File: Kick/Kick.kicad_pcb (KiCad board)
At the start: 4 copper layers, 11 parts, among them J1 CN1 / J11, J2 CN2 / J12, U0 NOIP1SN1300A-QTI, U1 NOIP1SN1300A-QTI, U2 NX3L4053, U3 NX3L4053, U4 MIC5504-1.8YM5

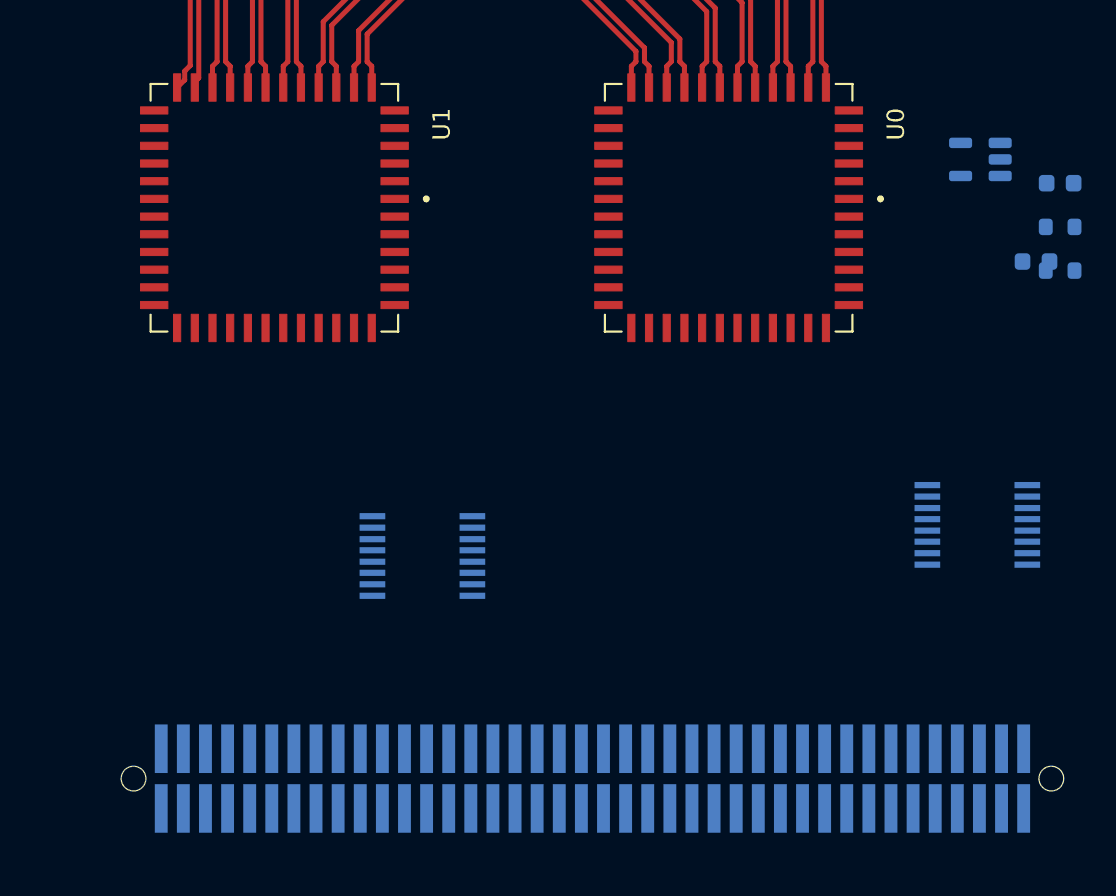
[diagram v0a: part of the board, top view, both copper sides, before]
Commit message: optimized placement of via next to the 2 NOIP2
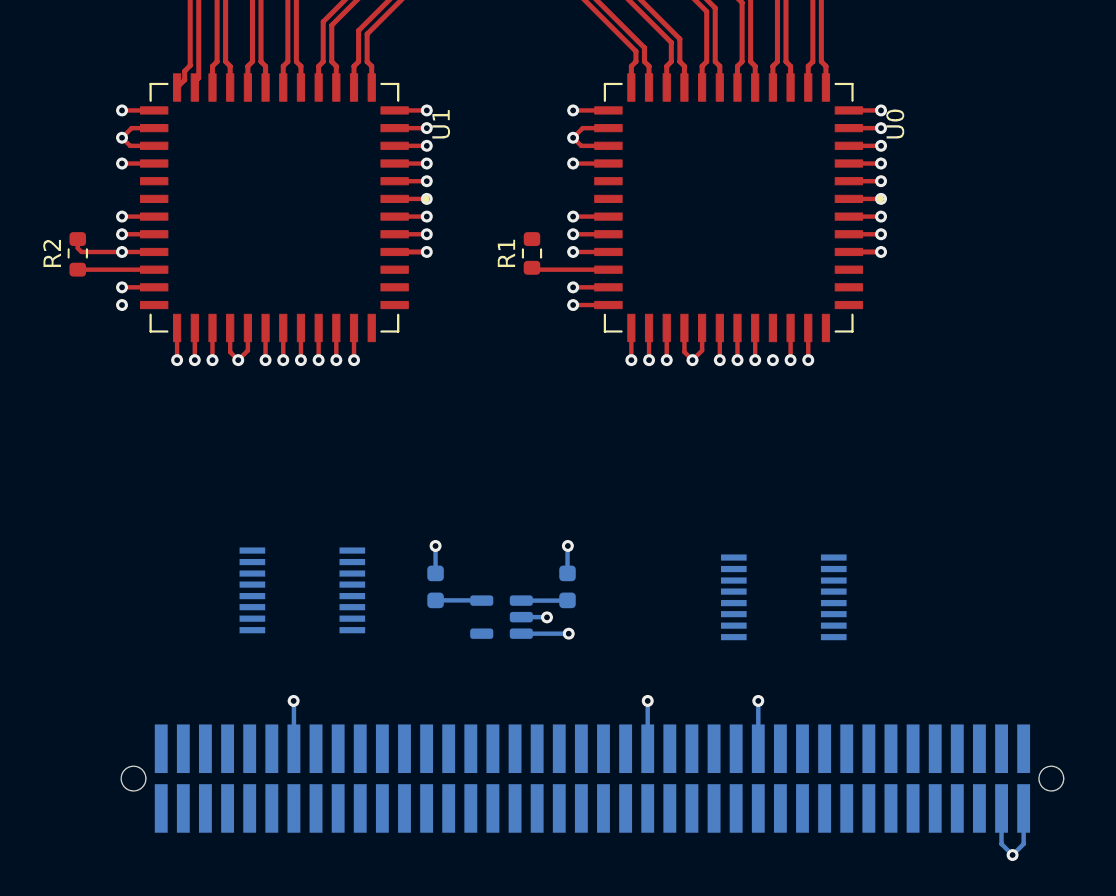
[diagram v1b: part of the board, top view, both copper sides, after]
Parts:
- R1, R2: moved to F.Cu
- moved R2 56.4 mm to (67.0, 72.0), turned to 90 degrees
- moved C2 42.7 mm to (87.6, 91.2), turned to 90 degrees
- moved U3 38.9 mm to (80.0, 91.4), turned to 0 degrees
- moved U4 38.0 mm to (91.4, 92.9)
- moved C1 32.8 mm to (95.2, 91.2), turned to 90 degrees
- moved R1 30.4 mm to (93.1, 72.0), turned to 90 degrees
- moved U2 20.9 mm to (107.6, 91.8)
- moved J1 1.06 mm to (97.1, 102.2), turned to 0 degrees
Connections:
- U0 pad 46: /reset0_N -> /resetn_0
- U2 pad 1: +3.3V -> +3V3
- U2 pad 3: +3.3V -> +3V3
- U3 pad 1: +3.3V -> +3V3
- U3 pad 3: +3.3V -> +3V3
- U4 pad 3: +3.3V -> +3V3
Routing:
- net GND: track 0.00 -> 61.3 mm, vias 0 -> 25
- net /vdd33_0: track 0.00 -> 8.35 mm, vias 0 -> 4
- net /vddpix_0: track 0.00 -> 7.39 mm, vias 0 -> 4
- net /vddpix_1: track 0.00 -> 7.39 mm, vias 0 -> 4
- net /vdd33_1: track 0.00 -> 7.39 mm, vias 0 -> 4
- net /vdd18_0: track 0.00 -> 5.90 mm, vias 0 -> 3
- net /vdd18_1: track 0.00 -> 5.54 mm, vias 0 -> 3
- net +3V3: track 0.00 -> 5.38 mm, vias 0 -> 1
- net Net-(U0-IBIAS_MASTER): track 0.00 -> 4.46 mm
- net Net-(U1-IBIAS_MASTER): track 0.00 -> 4.39 mm
- net /miso: track 0.00 -> 3.74 mm, vias 0 -> 2
- net /sck: track 0.00 -> 3.69 mm, vias 0 -> 2
- net /mosi: track 0.00 -> 3.69 mm, vias 0 -> 2
- net +1V8: track 0.00 -> 2.74 mm
- net /noip_clk_0: track 0.00 -> 2.03 mm, vias 0 -> 1
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- added copper zone on In2.Cu, net +3V3

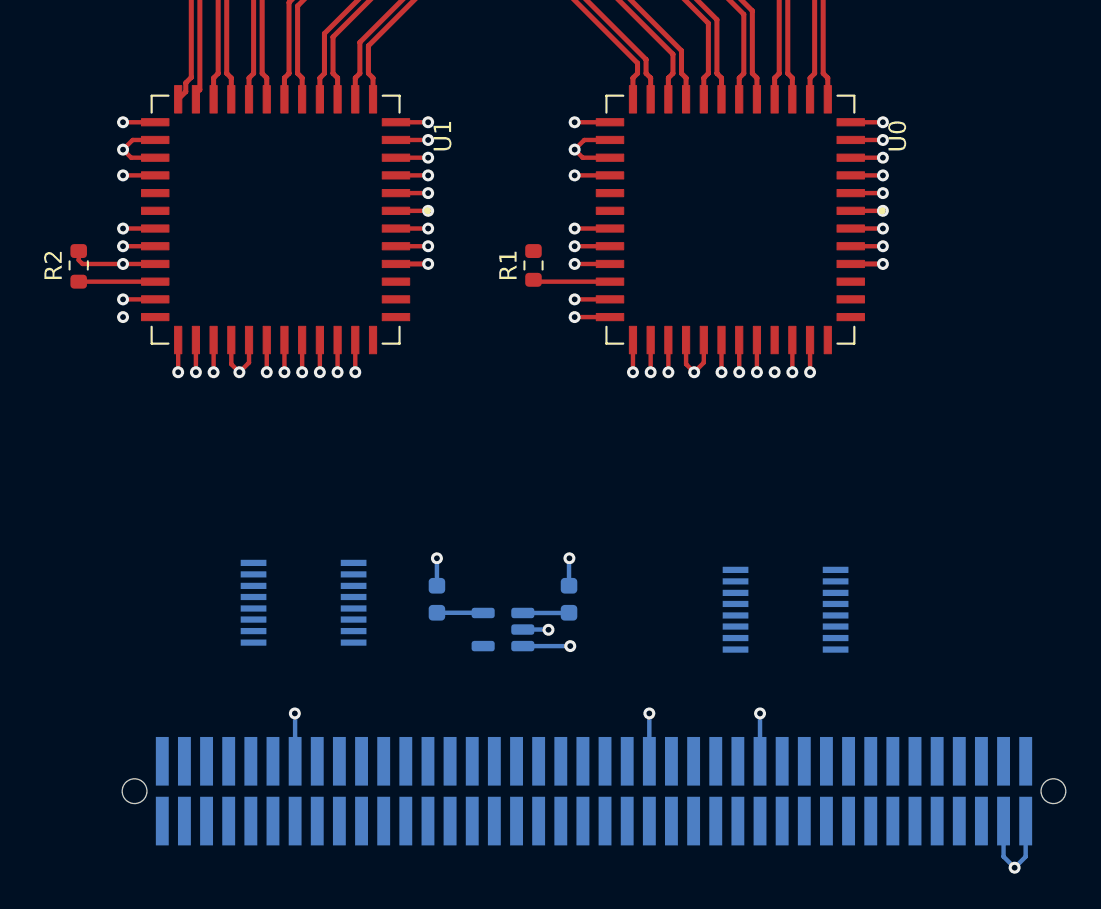
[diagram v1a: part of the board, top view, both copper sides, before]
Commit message: routed U1's side and power supply.
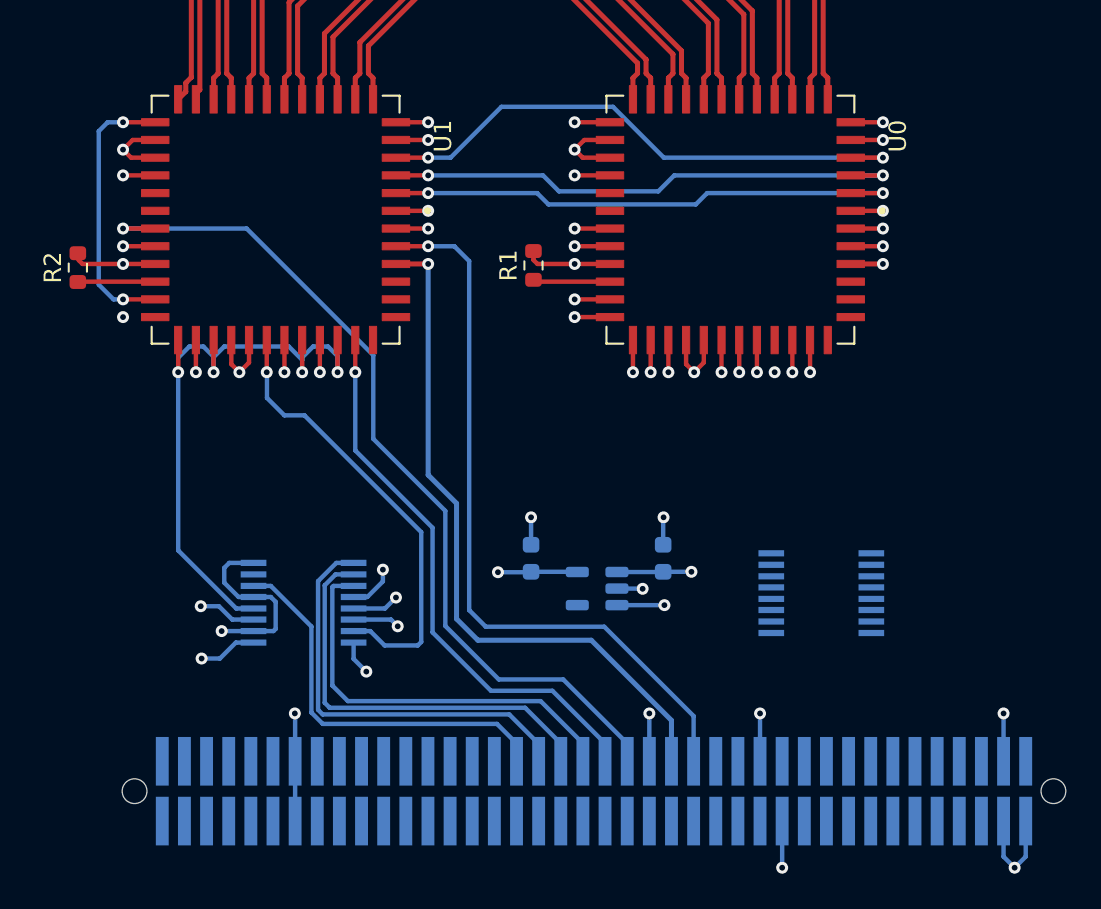
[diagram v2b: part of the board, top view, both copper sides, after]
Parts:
- moved C1 5.89 mm to (100.6, 88.8)
- moved C2 5.89 mm to (93.0, 88.8)
- moved U4 5.89 mm to (96.8, 90.6)
- moved U2 2.26 mm to (109.7, 90.8)
- moved R2 0.13 mm to (67.0, 72.2)
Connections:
- J1 pad 13: /vdd33_toggle_1 -> unconnected-(J1-Pin_13-Pad13)
- J1 pad 19: /vddpix_toggle_1 -> unconnected-(J1-Pin_19-Pad19)
- J1 pad 23: /sw_~{E}_1 -> unconnected-(J1-Pin_23-Pad23)
- J1 pad 28: /noip_clk_1 -> unconnected-(J1-Pin_28-Pad28)
- J1 pad 31: unconnected-(J1-Pin_31-Pad31) -> /ss_1
- J1 pad 32: /trigger0_1 -> unconnected-(J1-Pin_32-Pad32)
- J1 pad 33: unconnected-(J1-Pin_33-Pad33) -> /resetn_1
- J1 pad 37: /mosi -> /noip_clk_1
- J1 pad 38: /resetn_1 -> unconnected-(J1-Pin_38-Pad38)
- J1 pad 39: /miso -> /trigger0_1
- J1 pad 41: /sck -> /vdd18_toggle_1
- J1 pad 43: /ss_0 -> /vdd33_toggle_1
- J1 pad 45: /ss_1 -> /vddpix_toggle_1
- J1 pad 47: unconnected-(J1-Pin_47-Pad47) -> /sw_~{E}_1
- J1 pad 9: /vdd18_toggle_1 -> unconnected-(J1-Pin_9-Pad9)
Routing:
- net /vdd18_1: track 5.54 -> 66.5 mm, vias 3 -> 4
- net /vdd33_1: track 7.39 -> 60.9 mm
- net /noip_clk_1: track 1.85 -> 50.7 mm
- net /ss_1: track 1.85 -> 42.6 mm
- net /resetn_1: track 1.85 -> 40.0 mm
- net /trigger0_1: track 1.85 -> 32.2 mm
- net /vddpix_1: track 7.39 -> 37.5 mm
- net /sck: track 3.69 -> 32.2 mm
- net /miso: track 3.74 -> 30.6 mm
- net /mosi: track 3.69 -> 30.3 mm
- net /vddpix_toggle_1: track 0.00 -> 24.3 mm
- net /vdd33_toggle_1: track 0.00 -> 24.2 mm
- net /vdd18_toggle_1: track 0.00 -> 23.7 mm
- net /sw_~{E}_1: track 0.00 -> 22.7 mm
- net GND: track 61.3 -> 83.8 mm, vias 25 -> 28
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
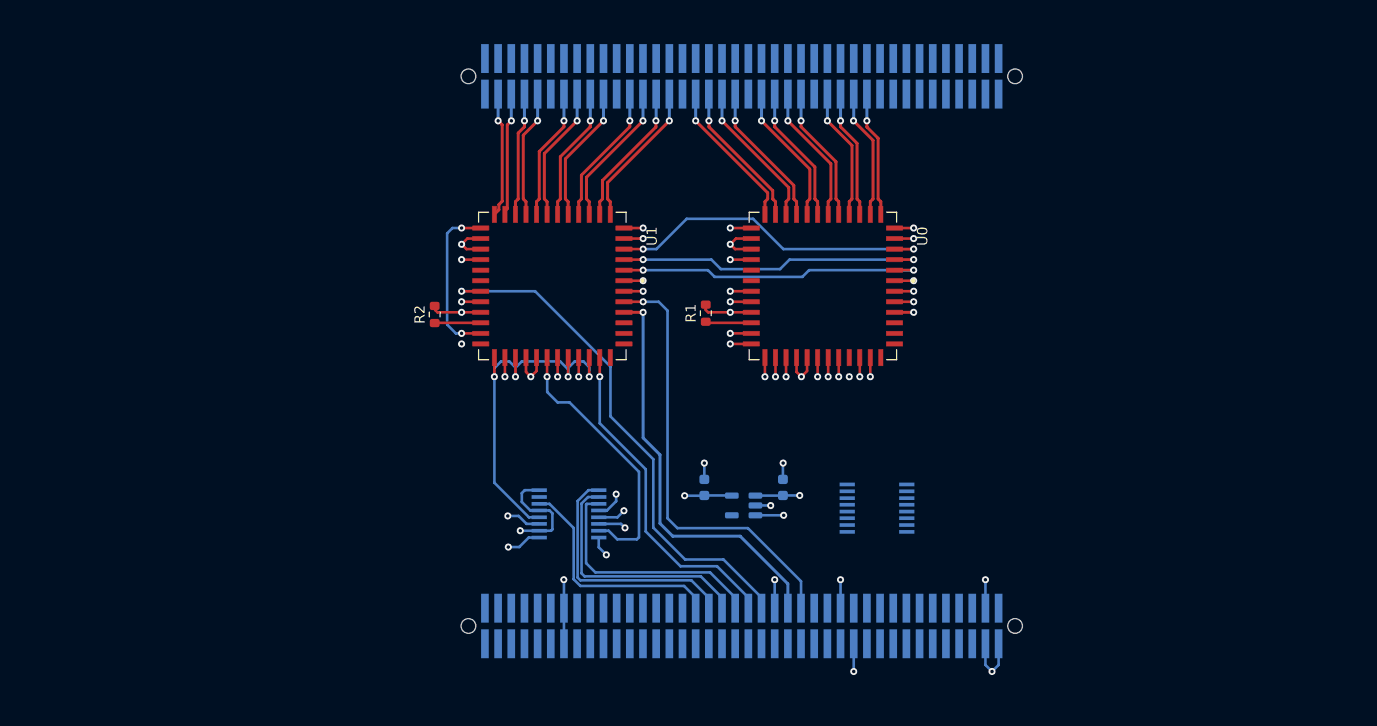
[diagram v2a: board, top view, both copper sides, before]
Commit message: preliminary routing (lacking spi and monitors), prior to setting correct distance between sensors
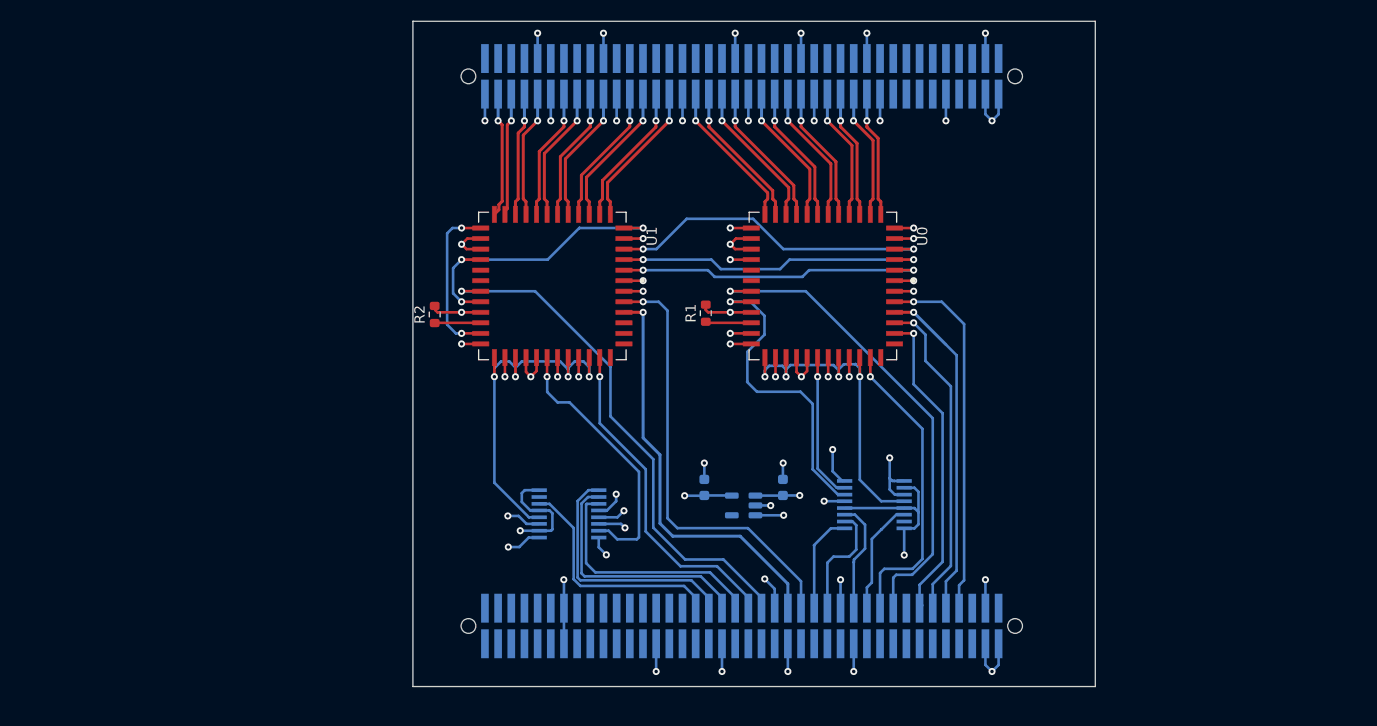
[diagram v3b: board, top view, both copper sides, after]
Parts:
- moved U2 0.42 mm to (109.4, 90.5)
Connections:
- J1 pad 11: /vdd33_toggle_0 -> /monitor1_0
- J1 pad 13: unconnected-(J1-Pin_13-Pad13) -> /monitor0_0
- J1 pad 17: /vddpix_toggle_0 -> /noip_clk_0
- J1 pad 19: unconnected-(J1-Pin_19-Pad19) -> /trigger0_0
- J1 pad 23: unconnected-(J1-Pin_23-Pad23) -> /vdd18_toggle_0
- J1 pad 26: /noip_clk_0 -> unconnected-(J1-Pin_26-Pad26)
- J1 pad 27: unconnected-(J1-Pin_27-Pad27) -> /vdd33_toggle_0
- J1 pad 29: unconnected-(J1-Pin_29-Pad29) -> /vddpix_toggle_0
- J1 pad 30: /trigger0_0 -> unconnected-(J1-Pin_30-Pad30)
- J1 pad 36: /resetn_0 -> unconnected-(J1-Pin_36-Pad36)
- J1 pad 7: /vdd18_toggle_0 -> /ss_0
- J1 pad 9: unconnected-(J1-Pin_9-Pad9) -> /resetn_0
- U0 pad 44: unconnected-(U0-MONITOR0-Pad44) -> /monitor0_0
- U0 pad 45: unconnected-(U0-MONITOR1-Pad45) -> /monitor1_0
- U1 pad 44: unconnected-(U1-MONITOR0-Pad44) -> /monitor1_0
- U1 pad 45: unconnected-(U1-MONITOR1-Pad45) -> /monitor1_1
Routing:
- net GND: track 83.8 -> 150.6 mm, vias 28 -> 46
- net /vdd18_0: track 5.90 -> 66.2 mm
- net /vdd33_0: track 8.35 -> 56.9 mm
- net /noip_clk_0: track 2.03 -> 47.4 mm
- net /ss_0: track 1.85 -> 35.2 mm
- net /monitor1_0: track 0.00 -> 31.6 mm, vias 0 -> 1
- net /monitor0_0: track 0.00 -> 30.8 mm, vias 0 -> 1
- net /resetn_0: track 1.85 -> 32.5 mm
- net /vddpix_0: track 7.39 -> 35.7 mm
- net /trigger0_0: track 1.85 -> 29.5 mm
- net +1V8: track 13.8 -> 31.0 mm, vias 2 -> 3
- net +3V3: track 18.4 -> 30.7 mm, vias 6 -> 9
- net /vdd33_toggle_0: track 0.00 -> 11.3 mm
- net /vdd33_1: track 60.9 -> 72.2 mm
- net /sw_~{E}_0: track 0.00 -> 11.0 mm
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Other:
- board outline added: 65.8 x 64.2 mm

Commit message: repositioned sensors and rerouted diff pairs
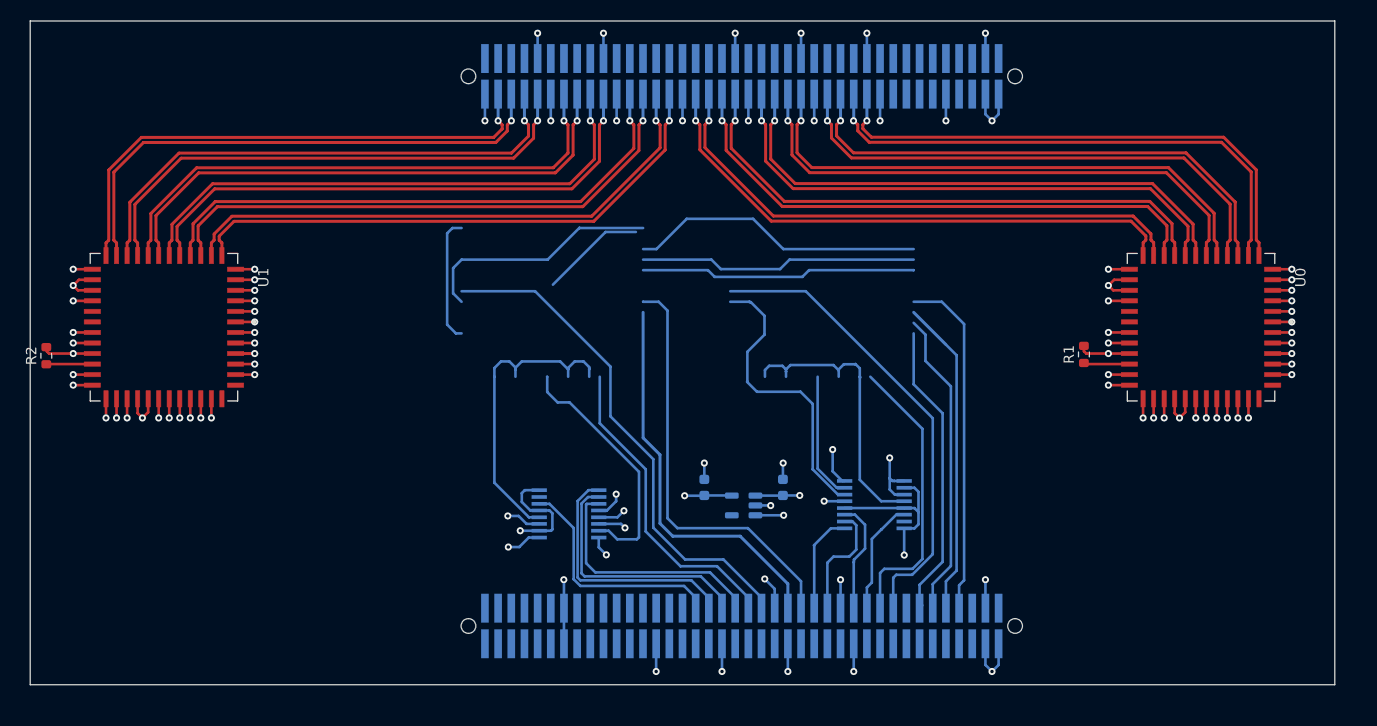
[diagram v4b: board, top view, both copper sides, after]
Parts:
- moved R2 37.7 mm to (29.6, 76.2)
- moved U1 37.7 mm to (40.9, 73.4)
- moved U0 36.7 mm to (140.9, 73.4)
- moved R1 36.7 mm to (129.6, 76.0)
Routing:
- net /dout0_1_P: track 13.6 -> 54.1 mm
- net /clkout1_P: track 13.8 -> 54.0 mm
- net /dout0_1_N: track 14.0 -> 54.1 mm
- net /dout3_0_N: track 14.0 -> 54.1 mm
- net /dout1_1_P: track 12.9 -> 52.9 mm
- net /dout2_1_P: track 12.7 -> 52.6 mm
- net /clkout1_N: track 14.2 -> 54.0 mm
- net /sync0_N: track 14.3 -> 54.0 mm
- net /dout3_0_P: track 14.4 -> 54.1 mm
- net /dout1_1_N: track 13.2 -> 52.9 mm
- net /dout2_1_N: track 13.0 -> 52.6 mm
- net /sync1_N: track 11.9 -> 51.5 mm
- net /dout2_0_N: track 13.3 -> 52.9 mm
- net /dout1_0_N: track 13.1 -> 52.6 mm
- net /sync0_P: track 14.6 -> 54.0 mm
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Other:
- board size 65.8 x 64.2 mm -> 125.8 x 64 mm
